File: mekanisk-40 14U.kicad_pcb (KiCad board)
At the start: 2 copper layers, 266.7 x 76.2 mm, 141 parts, among them J2 USB_C_Receptacle_USB2.0, Q1 2N7002, SW1 RST, U1 USBLC6-2SC6, U2 XC6206PxxxMR-Regulator_Linear, U3 STM32F072C8Tx

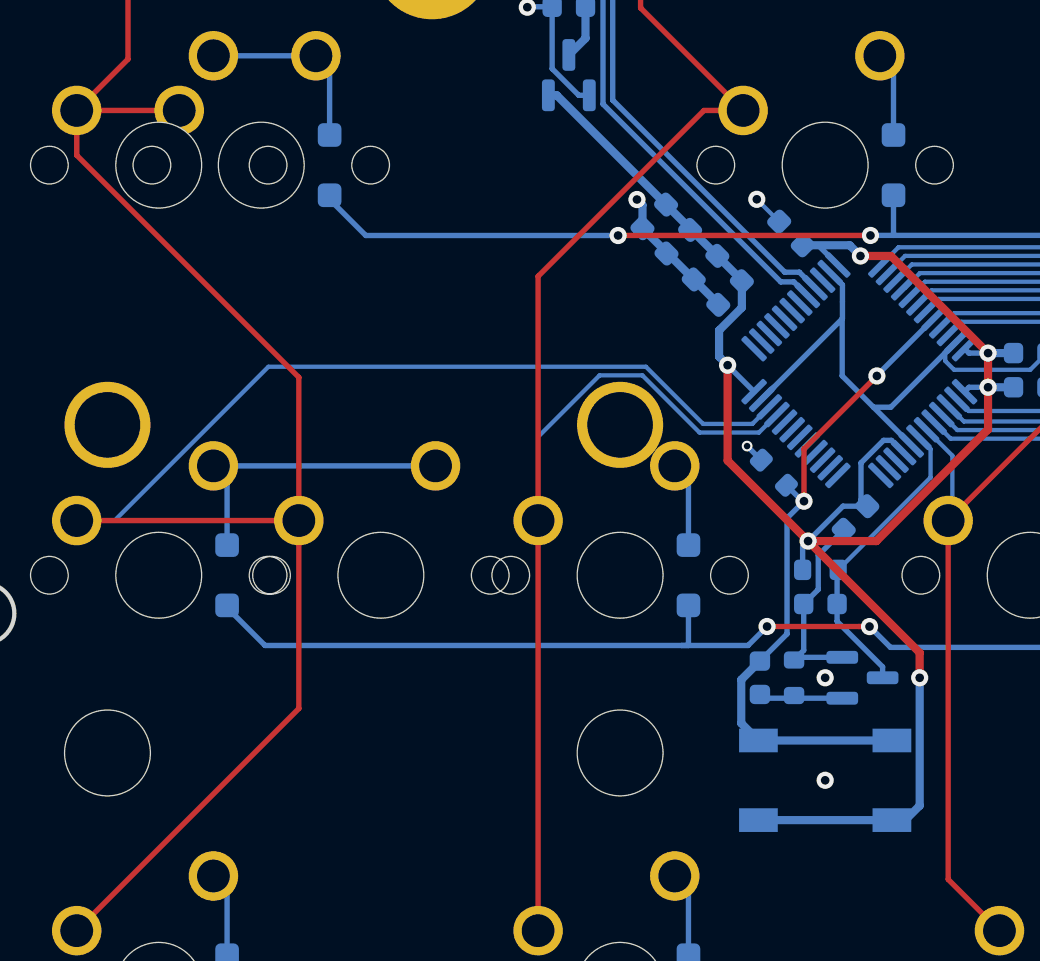
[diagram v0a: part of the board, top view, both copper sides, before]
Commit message: changed routing and reset button placement on 13u
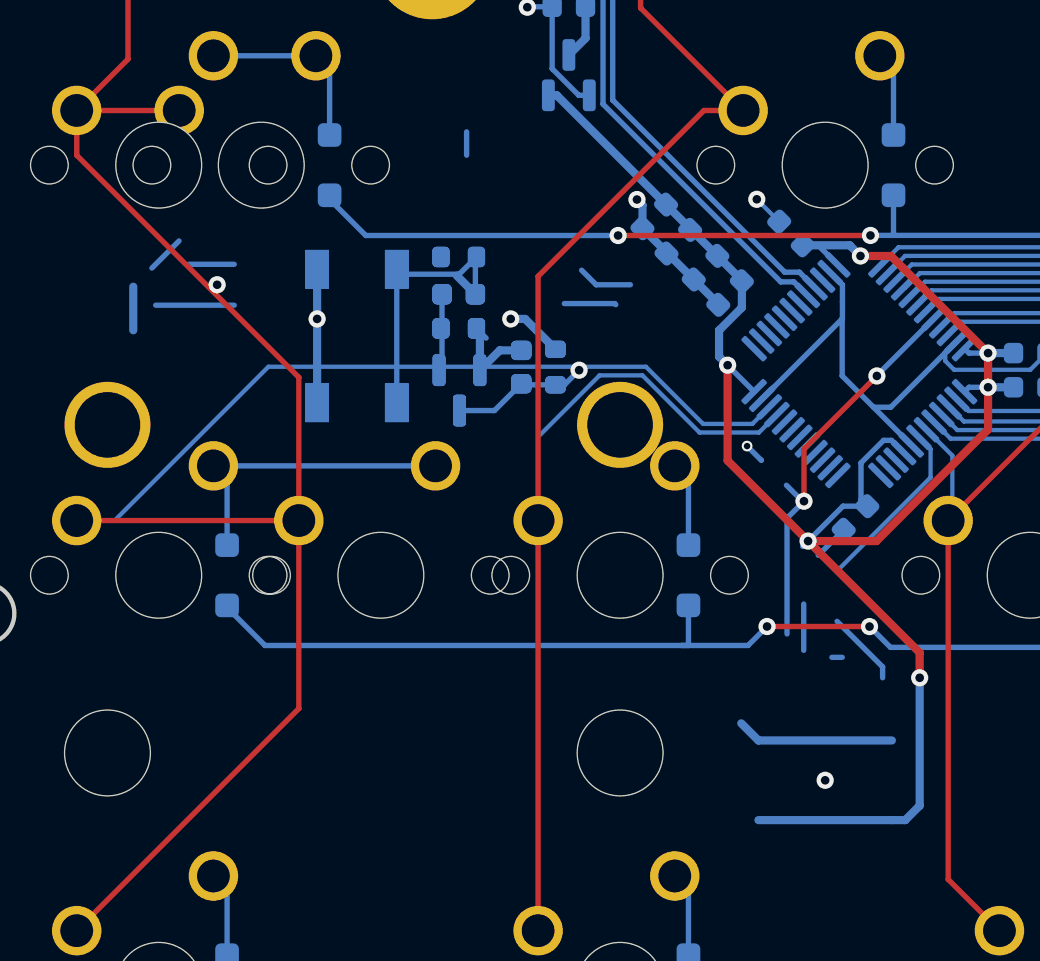
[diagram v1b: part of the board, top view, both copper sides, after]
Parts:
- added C10: 1u, Capacitor_SMD:C_0603_1608Metric, B.Cu at (44.1, 69.7)
- added C11: 4.7u, Capacitor_SMD:C_0603_1608Metric, B.Cu at (41.2, 66.3)
- added Q1: 2N7002, Package_TO_SOT_SMD:SOT-23, B.Cu at (41.3, 70.8)
- added R3: 10k, Resistor_SMD:R_0603_1608Metric, B.Cu at (41.2, 64.6)
- added R4: 10k, Resistor_SMD:R_0603_1608Metric, B.Cu at (45.7, 69.7)
- added R5: 100k, Resistor_SMD:R_0603_1608Metric, B.Cu at (41.2, 67.9)
- added SW1: RST, Button_Switch_SMD:SW_SPST_SKQG_WithoutStem, B.Cu at (36.5, 68.3)
- moved SW1 30.0 mm to (36.5, 68.3), turned to 90 degrees
- moved Q1 23.0 mm to (41.3, 70.8), turned to -90 degrees
- moved C11 22.7 mm to (41.2, 66.3), turned to 180 degrees
- moved R5 22.5 mm to (41.2, 67.9), turned to 0 degrees
- moved R3 17.7 mm to (41.2, 64.6), turned to 180 degrees
- moved C10 17.7 mm to (44.1, 69.7), turned to -90 degrees
- moved R4 15.5 mm to (45.7, 69.7), turned to -90 degrees
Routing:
- net BOOT0: track 31.0 -> 43.1 mm
- net +3V3: track 91.2 -> 98.9 mm, vias 6 -> 8
- net NRST: track 14.1 -> 20.4 mm, vias 0 -> 1
- net GND: track 82.1 -> 87.5 mm
- net Net-(Q1-G): track 3.90 -> 7.48 mm

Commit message: update
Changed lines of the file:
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@@
     (fp_arc (start 8.53125 -5.499999) (mid 8.677685 -5.853565) (end 9.03125 -5.999999)
       (stroke (width 0.05) (type solid)) (layer "Eco2.User"))
-    (fp_arc (start 9.03125 8.000001) (mid 8.677729 7.853537) (end 8.53125 7.500001)
+    (fp_arc (start 9.03125 8.000001) (mid 8.677693 7.853543) (end 8.53125 7.500001)
       (stroke (width 0.05) (type solid)) (layer "Eco2.User"))
-    (fp_arc (start 14.780039 -5.999999) (mid 15.133567 -5.853539) (end 15.280039 -5.499999)
+    (fp_arc (start 14.780039 -5.999999) (mid 15.133602 -5.853545) (end 15.280039 -5.499999)
       (stroke (width 0.05) (type solid)) (layer "Eco2.User"))
-    (fp_arc (start 15.28125 7.500001) (mid 15.134806 7.853571) (end 14.78125 8.000001)
+    (fp_arc (start 15.28125 7.500001) (mid 15.1348 7.853536) (end 14.78125 8.000001)
       (stroke (width 0.05) (type solid)) (layer "Eco2.User"))
     (pad "" thru_hole circle (at -11.90625 -6.985) (size 4 4) (drill 3.048) (layers "*.Cu" "B.Mask"))
@@
     (fp_arc (start 8.53125 -5.499999) (mid 8.677685 -5.853565) (end 9.03125 -5.999999)
       (stroke (width 0.05) (type solid)) (layer "Eco2.User"))
-    (fp_arc (start 9.03125 8.000001) (mid 8.677729 7.853537) (end 8.53125 7.500001)
+    (fp_arc (start 9.03125 8.000001) (mid 8.677693 7.853543) (end 8.53125 7.500001)
       (stroke (width 0.05) (type solid)) (layer "Eco2.User"))
-    (fp_arc (start 14.780039 -5.999999) (mid 15.133567 -5.853539) (end 15.280039 -5.499999)
+    (fp_arc (start 14.780039 -5.999999) (mid 15.133602 -5.853545) (end 15.280039 -5.499999)
       (stroke (width 0.05) (type solid)) (layer "Eco2.User"))
-    (fp_arc (start 15.28125 7.500001) (mid 15.134806 7.853571) (end 14.78125 8.000001)
+    (fp_arc (start 15.28125 7.500001) (mid 15.1348 7.853536) (end 14.78125 8.000001)
       (stroke (width 0.05) (type solid)) (layer "Eco2.User"))
     (pad "" thru_hole circle (at -11.90625 -6.985) (size 4 4) (drill 3.048) (layers "*.Cu" "B.Mask"))
@@
     (fp_arc (start 8.53125 -5.499999) (mid 8.677685 -5.853565) (end 9.03125 -5.999999)
       (stroke (width 0.05) (type solid)) (layer "Eco2.User"))
-    (fp_arc (start 9.03125 8.000001) (mid 8.677729 7.853537) (end 8.53125 7.500001)
+    (fp_arc (start 9.03125 8.000001) (mid 8.677693 7.853543) (end 8.53125 7.500001)
       (stroke (width 0.05) (type solid)) (layer "Eco2.User"))
-    (fp_arc (start 14.780039 -5.999999) (mid 15.133567 -5.853539) (end 15.280039 -5.499999)
+    (fp_arc (start 14.780039 -5.999999) (mid 15.133602 -5.853545) (end 15.280039 -5.499999)
       (stroke (width 0.05) (type solid)) (layer "Eco2.User"))
-    (fp_arc (start 15.28125 7.500001) (mid 15.134806 7.853571) (end 14.78125 8.000001)
+    (fp_arc (start 15.28125 7.500001) (mid 15.1348 7.853536) (end 14.78125 8.000001)
       (stroke (width 0.05) (type solid)) (layer "Eco2.User"))
     (pad "" thru_hole circle (at -11.90625 -6.985 180) (size 4 4) (drill 3.048) (layers "*.Cu" "B.Mask"))
@@
     (fp_arc (start 8.53125 -5.499999) (mid 8.677685 -5.853565) (end 9.03125 -5.999999)
       (stroke (width 0.05) (type solid)) (layer "Eco2.User"))
-    (fp_arc (start 9.03125 8.000001) (mid 8.677729 7.853537) (end 8.53125 7.500001)
+    (fp_arc (start 9.03125 8.000001) (mid 8.677693 7.853543) (end 8.53125 7.500001)
       (stroke (width 0.05) (type solid)) (layer "Eco2.User"))
-    (fp_arc (start 14.780039 -5.999999) (mid 15.133567 -5.853539) (end 15.280039 -5.499999)
+    (fp_arc (start 14.780039 -5.999999) (mid 15.133602 -5.853545) (end 15.280039 -5.499999)
       (stroke (width 0.05) (type solid)) (layer "Eco2.User"))
-    (fp_arc (start 15.28125 7.500001) (mid 15.134806 7.853571) (end 14.78125 8.000001)
+    (fp_arc (start 15.28125 7.500001) (mid 15.1348 7.853536) (end 14.78125 8.000001)
       (stroke (width 0.05) (type solid)) (layer "Eco2.User"))
     (pad "" thru_hole circle (at -11.90625 -6.985 180) (size 4 4) (drill 3.048) (layers "*.Cu" "B.Mask"))
@@
     (fp_arc (start 8.53125 -5.499999) (mid 8.677685 -5.853565) (end 9.03125 -5.999999)
       (stroke (width 0.05) (type solid)) (layer "Eco2.User"))
-    (fp_arc (start 9.03125 8.000001) (mid 8.677729 7.853537) (end 8.53125 7.500001)
+    (fp_arc (start 9.03125 8.000001) (mid 8.677693 7.853543) (end 8.53125 7.500001)
       (stroke (width 0.05) (type solid)) (layer "Eco2.User"))
-    (fp_arc (start 14.780039 -5.999999) (mid 15.133567 -5.853539) (end 15.280039 -5.499999)
+    (fp_arc (start 14.780039 -5.999999) (mid 15.133602 -5.853545) (end 15.280039 -5.499999)
       (stroke (width 0.05) (type solid)) (layer "Eco2.User"))
-    (fp_arc (start 15.28125 7.500001) (mid 15.134806 7.853571) (end 14.78125 8.000001)
+    (fp_arc (start 15.28125 7.500001) (mid 15.1348 7.853536) (end 14.78125 8.000001)
       (stroke (width 0.05) (type solid)) (layer "Eco2.User"))
     (pad "" thru_hole circle (at -11.90625 -6.985) (size 4 4) (drill 3.048) (layers "*.Cu" "B.Mask"))
@@
   (segment (start 163.98875 38.735) (end 163.98875 53.0225) (width 0.25) (layer "F.Cu") (net 57))
   (segment (start 168.75125 57.785) (end 168.75125 67.31) (width 0.25) (layer "F.Cu") (net 57))
-  (segment (start 70.713034 69.0361) (end 69.278102 67.601167) (width 0.2) (layer "B.Cu") (net 57))
-  (segment (start 69.278102 67.601167) (end 64.572457 67.601167) (width 0.2) (layer "B.Cu") (net 57))
-  (segment (start 64.572457 67.601167) (end 64.029519 68.144105) (width 0.2) (layer "B.Cu") (net 57))
-  (segment (start 151.42735 69.0361) (end 70.713034 69.0361) (width 0.2) (layer "B.Cu") (net 57))
+  (segment (start 69.017441 67.340507) (end 64.833117 67.340507) (width 0.2) (layer "B.Cu") (net 57))
+  (segment (start 64.833117 67.340507) (end 64.029519 68.144105) (width 0.2) (layer "B.Cu") (net 57))
+  (segment (start 70.713034 69.0361) (end 69.017441 67.340507) (width 0.2) (layer "B.Cu") (net 57))
   (segment (start 159.22625 76.835) (end 151.42735 69.0361) (width 0.2) (layer "B.Cu") (net 57))
+  (segment (start 151.42735 69.0361) (end 70.713034 69.0361) (width 0.2) (layer "B.Cu") (net 57))
   (segment (start 187.80125 57.785) (end 187.80125 67.31) (width 0.25) (layer "F.Cu") (net 58))
   (segment (start 183.03875 38.735) (end 183.03875 53.0225) (width 0.25) (layer "F.Cu") (net 58))
   (segment (start 183.03875 53.0225) (end 187.80125 57.785) (width 0.25) (layer "F.Cu") (net 58))
   (segment (start 187.80125 67.31) (end 178.27625 76.835) (width 0.25) (layer "F.Cu") (net 58))
-  (segment (start 69.443787 67.201167) (end 64.265349 67.201167) (width 0.2) (layer "B.Cu") (net 58))
-  (segment (start 64.265349 67.201167) (end 63.675965 67.790551) (width 0.2) (layer "B.Cu") (net 58))
-  (segment (start 70.87872 68.6361) (end 69.443787 67.201167) (width 0.2) (layer "B.Cu") (net 58))
-  (segment (start 178.27625 76.835) (end 170.07735 68.6361) (width 0.2) (layer "B.Cu") (net 58))
+  (segment (start 64.526009 66.940507) (end 63.675965 67.790551) (width 0.2) (layer "B.Cu") (net 58))
+  (segment (start 69.183127 66.940507) (end 64.526009 66.940507) (width 0.2) (layer "B.Cu") (net 58))
   (segment (start 170.07735 68.6361) (end 70.87872 68.6361) (width 0.2) (layer "B.Cu") (net 58))
+  (segment (start 70.87872 68.6361) (end 69.183127 66.940507) (width 0.2) (layer "B.Cu") (net 58))
+  (segment (start 178.27625 76.835) (end 170.07735 68.6361) (width 0.2) (layer "B.Cu") (net 58))
   (segment (start 206.85125 57.785) (end 206.85125 67.31) (width 0.25) (layer "F.Cu") (net 59))
   (segment (start 206.85125 67.31) (end 197.32625 76.835) (width 0.25) (layer "F.Cu") (net 59))
